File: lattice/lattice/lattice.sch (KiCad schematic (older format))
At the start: 107 parts, among them J1 AudioJack2, J10 AudioJack2, J11 AudioJack2, J12 AudioJack2, J13 AudioJack2, J14 AudioJack2, J15 AudioJack2, J16 Conn_02x05_Counter_Clockwise, J17 Conn_01x10, J18 Conn_01x10, J19 Conn_01x08, J2 AudioJack2, J20 Conn_01x08, J21 Conn_01x07, J22 Conn_01x07, J23 Conn_01x07, J24 Conn_01x07, J3 AudioJack2, J4 AudioJack2, J5 AudioJack2, J6 AudioJack2, J7 AudioJack2, J8 AudioJack2, J9 Conn_02x08_Odd_Even, Q1 BC548, Q2 BC548, SW1 LP4OA1PBCT, U1 MCP6002-xP, U2 MCP6002-xP, U3 MCP6002-xP, U5 6N138, U6 LM4040LP-5, U7 74HC595

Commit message: Fixing wrong pin assignments for triggers and accents
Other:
- note removed: "Figure out which jacks go where"
- moved on the sheet: JP1, JP2
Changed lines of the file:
@@
 	1    0    0    -1
 $EndComp
-Text Notes 14100 5050 0    50   ~ 0
-Figure out which jacks go where
 Wire Wire Line
 	7650 5500 7750 5500
@@
 L Device:Jumper JP1
 U 1 1 6326F1A8
-P 11550 7100
-F 0 "JP1" H 11550 7364 50  0000 C CNN
-F 1 "Jumper" H 11550 7273 50  0000 C CNN
-F 2 "Connector_PinHeader_2.54mm:PinHeader_1x02_P2.54mm_Vertical" H 11550 7100 50  0001 C CNN
-F 3 "~" H 11550 7100 50  0001 C CNN
-	1    11550 7100
+P 12350 7150
+F 0 "JP1" H 12350 7414 50  0000 C CNN
+F 1 "Jumper" H 12350 7323 50  0000 C CNN
+F 2 "Connector_PinHeader_2.54mm:PinHeader_1x02_P2.54mm_Vertical" H 12350 7150 50  0001 C CNN
+F 3 "~" H 12350 7150 50  0001 C CNN
+	1    12350 7150
 	1    0    0    -1
 $EndComp
@@
 L Device:Jumper JP2
 U 1 1 63271078
-P 11550 7450
-F 0 "JP2" H 11550 7714 50  0000 C CNN
-F 1 "Jumper" H 11550 7623 50  0000 C CNN
-F 2 "Connector_PinHeader_2.54mm:PinHeader_1x02_P2.54mm_Vertical" H 11550 7450 50  0001 C CNN
-F 3 "~" H 11550 7450 50  0001 C CNN
-	1    11550 7450
+P 12350 7500
+F 0 "JP2" H 12350 7764 50  0000 C CNN
+F 1 "Jumper" H 12350 7673 50  0000 C CNN
+F 2 "Connector_PinHeader_2.54mm:PinHeader_1x02_P2.54mm_Vertical" H 12350 7500 50  0001 C CNN
+F 3 "~" H 12350 7500 50  0001 C CNN
+	1    12350 7500
 	1    0    0    -1
 $EndComp
@@
 L power:+12V #PWR0138
 U 1 1 6328FCE5
-P 11250 7100
-F 0 "#PWR0138" H 11250 6950 50  0001 C CNN
-F 1 "+12V" H 11265 7273 50  0000 C CNN
-F 2 "" H 11250 7100 50  0001 C CNN
-F 3 "" H 11250 7100 50  0001 C CNN
-	1    11250 7100
-	1    0    0    -1
-$EndComp
-Text Label 11850 7100 0    50   ~ 0
+P 12050 7150
+F 0 "#PWR0138" H 12050 7000 50  0001 C CNN
+F 1 "+12V" H 12065 7323 50  0000 C CNN
+F 2 "" H 12050 7150 50  0001 C CNN
+F 3 "" H 12050 7150 50  0001 C CNN
+	1    12050 7150
+	1    0    0    -1
+$EndComp
+Text Label 12650 7150 0    50   ~ 0
 ARDUINO_POWER_12v
-Text Label 11850 7450 0    50   ~ 0
+Text Label 12650 7500 0    50   ~ 0
 ARDUINO_POWER_5v
 Connection ~ 9950 2900
@@
 Text Label 13800 3300 0    50   ~ 0
 CH1A
+Text Label 13600 5400 0    50   ~ 0
+CH1B
 Text Label 13750 4000 0    50   ~ 0
-CH1B
-Text Label 13750 4700 0    50   ~ 0
 CH2A
-Text Label 13600 5400 0    50   ~ 0
+Text Label 13550 6100 0    50   ~ 0
 CH2B
-Text Label 13550 6100 0    50   ~ 0
+Text Label 13650 4700 0    50   ~ 0
 CH3A
 Text Label 13500 6800 0    50   ~ 0
@@
 Text Label 11150 7750 0    50   ~ 0
 5V_POWER_CONNECTOR
-Text Label 11250 7450 2    50   ~ 0
+Text Label 12050 7500 2    50   ~ 0
 5V_POWER_CONNECTOR
 Wire Wire Line

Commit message: More error-patching...
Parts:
- removed J16: Conn_02x05_Counter_Clockwise, Connector_PinHeader_2.54mm:PinHeader_2x05_P2.54mm_Vertical, symbol Connector_Generic:Conn_02x05_Counter_Clockwise
- added J16: Conn_02x05_Odd_Even, Connector_PinHeader_2.54mm:PinHeader_2x05_P2.54mm_Vertical, symbol Connector_Generic:Conn_02x05_Odd_Even
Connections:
- wire segments 308 -> 310
- no-connect marks 10 -> 9
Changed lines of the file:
@@
 EXT_MIDI_IN_PIN_5
-$Comp
-L Connector_Generic:Conn_02x05_Counter_Clockwise J16
-U 1 1 620B268B
-P 11850 5350
-F 0 "J16" H 11900 5767 50  0000 C CNN
-F 1 "Conn_02x05_Counter_Clockwise" H 11900 5676 50  0000 C CNN
-F 2 "Connector_PinHeader_2.54mm:PinHeader_2x05_P2.54mm_Vertical" H 11850 5350 50  0001 C CNN
-F 3 "~" H 11850 5350 50  0001 C CNN
-	1    11850 5350
-	1    0    0    -1
-$EndComp
 $Comp
 L power:+5V #PWR0161
@@
 	11650 5150 11650 5250
 Wire Wire Line
-	11650 5250 11650 5350
-Connection ~ 11650 5250
-Wire Wire Line
-	11650 5350 11650 5450
-Connection ~ 11650 5350
-Wire Wire Line
 	11650 5450 11650 5550
-Connection ~ 11650 5450
-Connection ~ 11650 5550
 $Comp
 L Reference_Voltage:LM4040LP-5 U6
@@
 Text Label 9250 3650 2    70   ~ 0
 IN_MIDI
-NoConn ~ 12150 5350
 $Comp
 L Transistor_BJT:BC548 Q1
@@
 	10350 7600 9850 7600
 Connection ~ 9850 7600
+Wire Wire Line
+	11650 5250 11550 5250
+Wire Wire Line
+	11550 5250 11550 5450
+Wire Wire Line
+	11550 5450 11650 5450
+$Comp
+L power:+5V #PWR0137
+U 1 1 615A568E
+P 11450 5350
+F 0 "#PWR0137" H 11450 5200 50  0001 C CNN
+F 1 "+5V" H 11465 5523 50  0000 C CNN
+F 2 "" H 11450 5350 50  0001 C CNN
+F 3 "" H 11450 5350 50  0001 C CNN
+	1    11450 5350
+	1    0    0    -1
+$EndComp
+$Comp
+L Connector_Generic:Conn_02x05_Odd_Even J16
+U 1 1 615E4142
+P 11850 5350
+F 0 "J16" H 11900 5767 50  0000 C CNN
+F 1 "Conn_02x05_Odd_Even" H 11900 5676 50  0000 C CNN
+F 2 "Connector_PinHeader_2.54mm:PinHeader_2x05_P2.54mm_Vertical" H 11850 5350 50  0001 C CNN
+F 3 "~" H 11850 5350 50  0001 C CNN
+	1    11850 5350
+	1    0    0    -1
+$EndComp
+Wire Wire Line
+	11450 5350 11650 5350
+Connection ~ 11650 5250
+Connection ~ 11650 5450
+Connection ~ 11650 5550
 $EndSCHEMATC

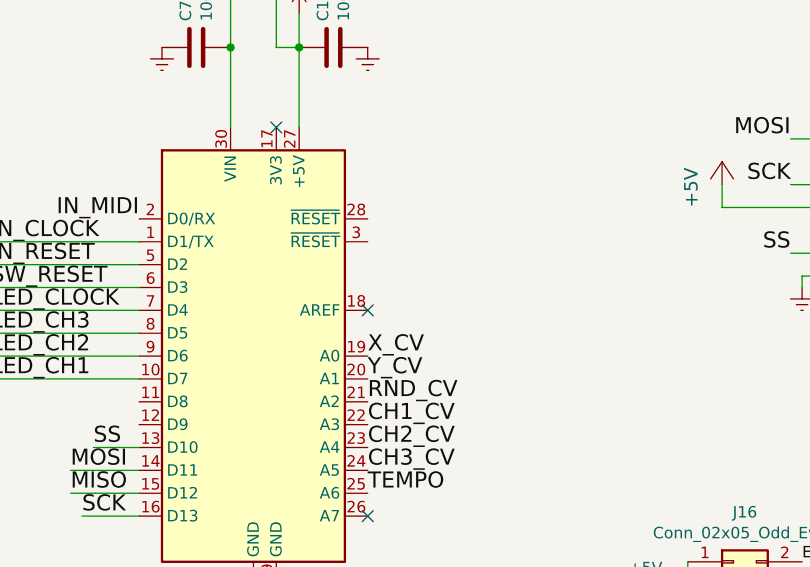
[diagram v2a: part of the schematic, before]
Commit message: Adding AREF decoupling capacitor
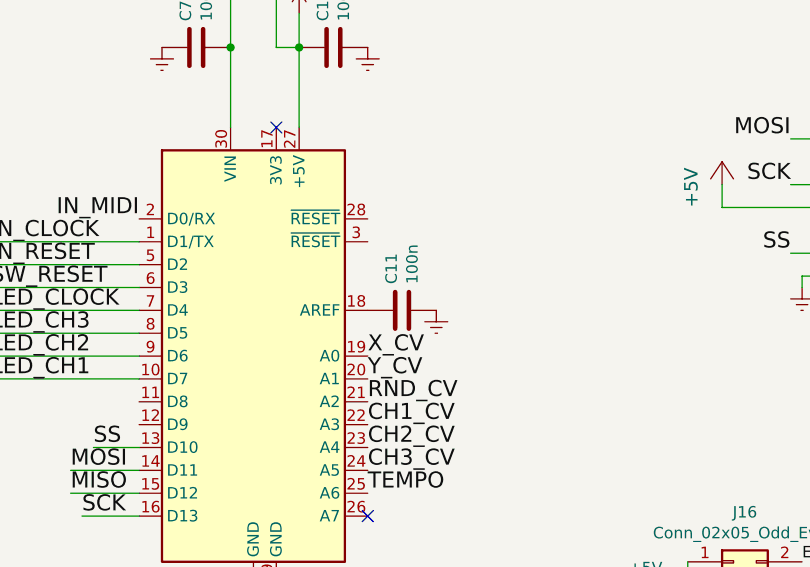
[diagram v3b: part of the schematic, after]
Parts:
- added C11: 100n, Capacitor_THT:C_Disc_D3.8mm_W2.6mm_P2.50mm, symbol Device:C
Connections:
- net Earth: now also C11.2
- net at A1.18 (AREF): now also C11.1
- no-connect marks 9 -> 8
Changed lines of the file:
@@
 Wire Wire Line
 	9850 2500 9850 2900
-NoConn ~ 10250 4050
 $Comp
 L Device:CP C10
@@
 Connection ~ 11650 5450
 Connection ~ 11650 5550
+$Comp
+L Device:C C11
+U 1 1 61672C60
+P 10400 4050
+F 0 "C11" H 10515 4096 50  0000 L CNN
+F 1 "100n" H 10515 4005 50  0000 L CNN
+F 2 "Capacitor_THT:C_Disc_D3.8mm_W2.6mm_P2.50mm" H 10438 3900 50  0001 C CNN
+F 3 "~" H 10400 4050 50  0001 C CNN
+	1    10400 4050
+	0    -1   -1   0
+$EndComp
+$Comp
+L power:Earth #PWR0139
+U 1 1 616A92C3
+P 10550 4050
+F 0 "#PWR0139" H 10550 3800 50  0001 C CNN
+F 1 "Earth" H 10550 3900 50  0001 C CNN
+F 2 "" H 10550 4050 50  0001 C CNN
+F 3 "~" H 10550 4050 50  0001 C CNN
+	1    10550 4050
+	1    0    0    -1
+$EndComp
 $EndSCHEMATC

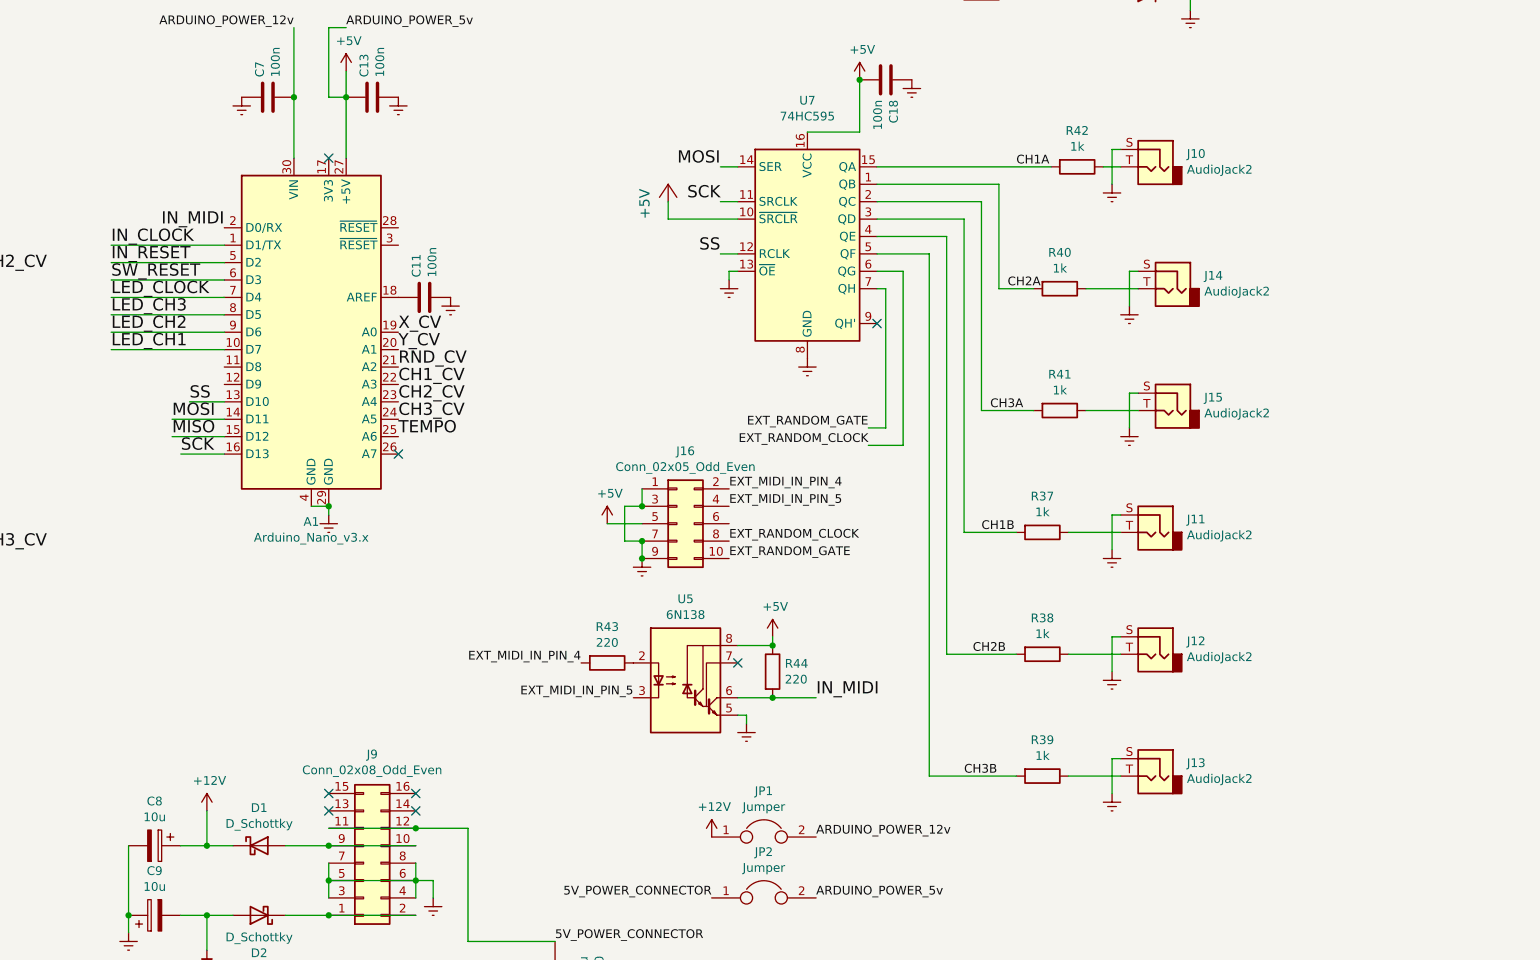
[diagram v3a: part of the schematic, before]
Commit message: Adding expansion ports from the Arduino
Not used in the default firmware, but if someone comes up with something neat....
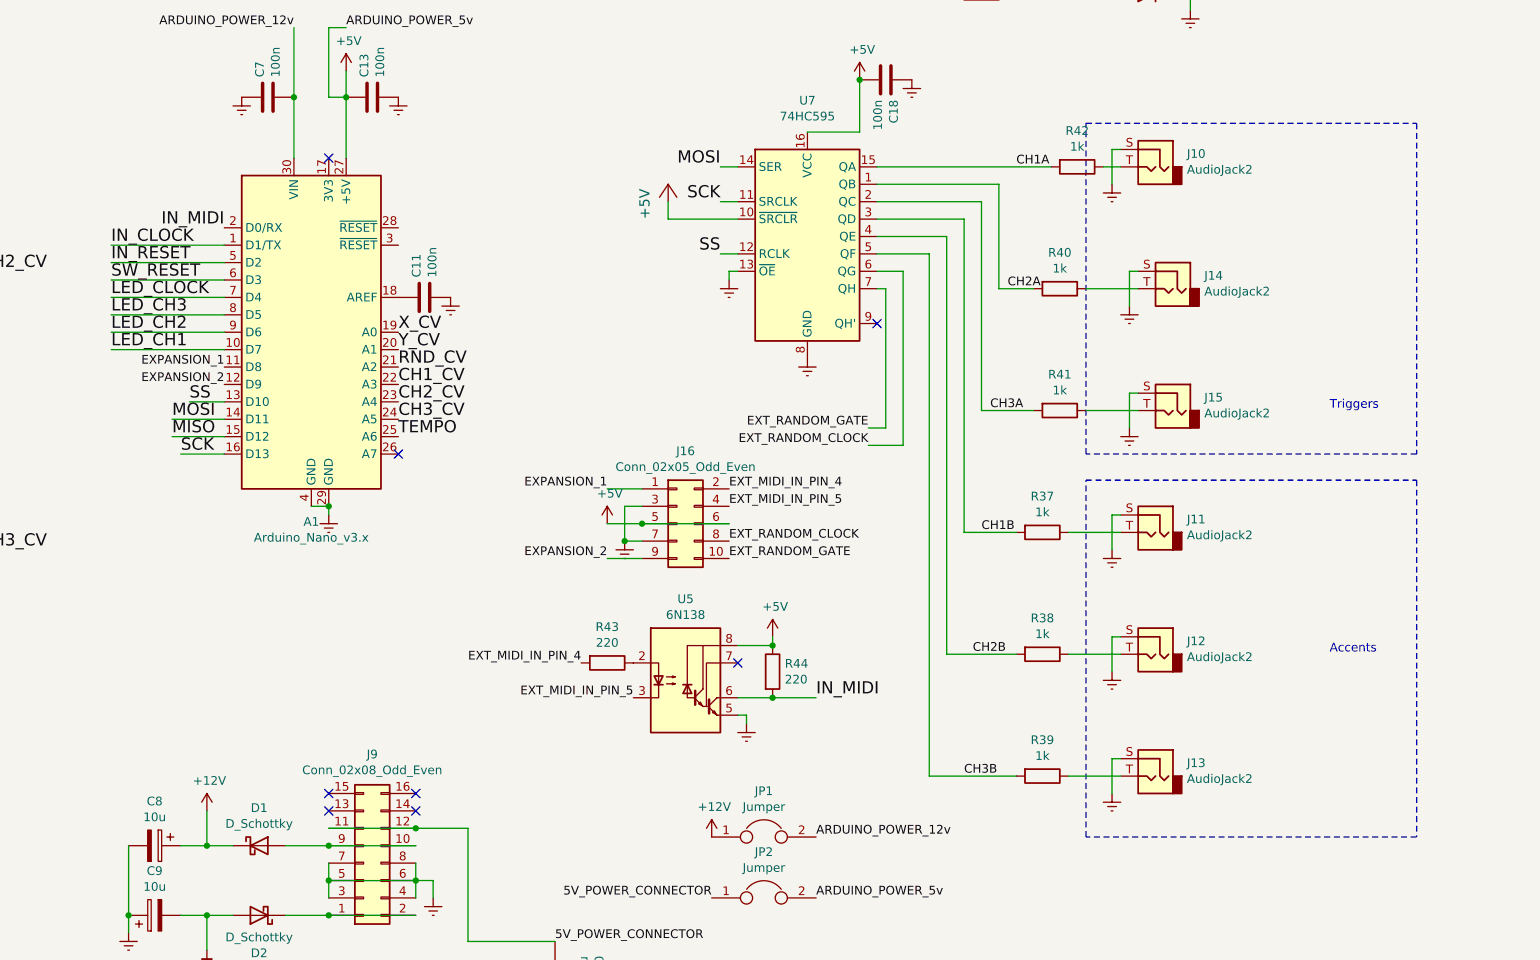
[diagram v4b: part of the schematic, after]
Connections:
- net +5V: now also J16.6 (Pin_6)
- net Earth: no longer J16.1 (Pin_1), J16.9 (Pin_9)
- net EXPANSION_1: now reaches A1.11 (D8)
- net EXPANSION_1: now also J16.1 (Pin_1)
- net EXPANSION_2: now reaches A1.12 (D9)
- net EXPANSION_2: now also J16.9 (Pin_9)
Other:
- note added: "Accents"
- note added: "Triggers"
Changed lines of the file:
@@
 L power:Earth #PWR0162
 U 1 1 62210E7D
-P 11650 5550
-F 0 "#PWR0162" H 11650 5300 50  0001 C CNN
-F 1 "Earth" H 11650 5400 50  0001 C CNN
-F 2 "" H 11650 5550 50  0001 C CNN
-F 3 "~" H 11650 5550 50  0001 C CNN
-	1    11650 5550
-	1    0    0    -1
-$EndComp
-Wire Wire Line
-	11650 5150 11650 5250
-Wire Wire Line
-	11650 5450 11650 5550
+P 11550 5450
+F 0 "#PWR0162" H 11550 5200 50  0001 C CNN
+F 1 "Earth" H 11550 5300 50  0001 C CNN
+F 2 "" H 11550 5450 50  0001 C CNN
+F 3 "~" H 11550 5450 50  0001 C CNN
+	1    11550 5450
+	1    0    0    -1
+$EndComp
 $Comp
 L Reference_Voltage:LM4040LP-5 U6
@@
 Wire Wire Line
 	11450 5350 11650 5350
-Connection ~ 11650 5250
-Connection ~ 11650 5450
-Connection ~ 11650 5550
 $Comp
 L Device:C C11
@@
 	1    0    0    -1
 $EndComp
+Text Notes 15600 4700 0    50   ~ 0
+Triggers
+Text Notes 15600 6100 0    50   ~ 0
+Accents
+Wire Notes Line
+	14200 5100 16100 5100
+Wire Notes Line
+	16100 5100 16100 7150
+Wire Notes Line
+	16100 7150 14200 7150
+Wire Notes Line
+	14200 7150 14200 5100
+Wire Notes Line
+	16100 4950 14200 4950
+Wire Notes Line
+	14200 4950 14200 3050
+Wire Notes Line
+	14200 3050 16100 3050
+Wire Notes Line
+	16100 3050 16100 4950
+Wire Wire Line
+	12150 5350 11650 5350
+Connection ~ 11650 5350
+Text Label 9250 4450 2    50   ~ 0
+EXPANSION_1
+Text Label 9250 4550 2    50   ~ 0
+EXPANSION_2
+Text Label 11450 5150 2    50   ~ 0
+EXPANSION_1
+Text Label 11450 5550 2    50   ~ 0
+EXPANSION_2
+Connection ~ 11550 5450
+Wire Wire Line
+	11450 5550 11650 5550
+Wire Wire Line
+	11450 5150 11650 5150
 $EndSCHEMATC
